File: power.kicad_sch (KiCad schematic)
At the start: 140 parts, among them Q10 SI7613DN-T1-GE3, Q2 BC817-25W, Q3 DZDH0401DW, Q4 DZDH0401DW, Q5 SI7613DN-T1-GE3, Q6 SI7613DN-T1-GE3, Q7 BC817-25W, Q8 BC817-25W, Q9 SI7613DN-T1-GE3, U1 LT8350RV#PBF, U2 MP2386GG, U3 TPS65983BAZBHR, U9 LM1117MP-25NOPB

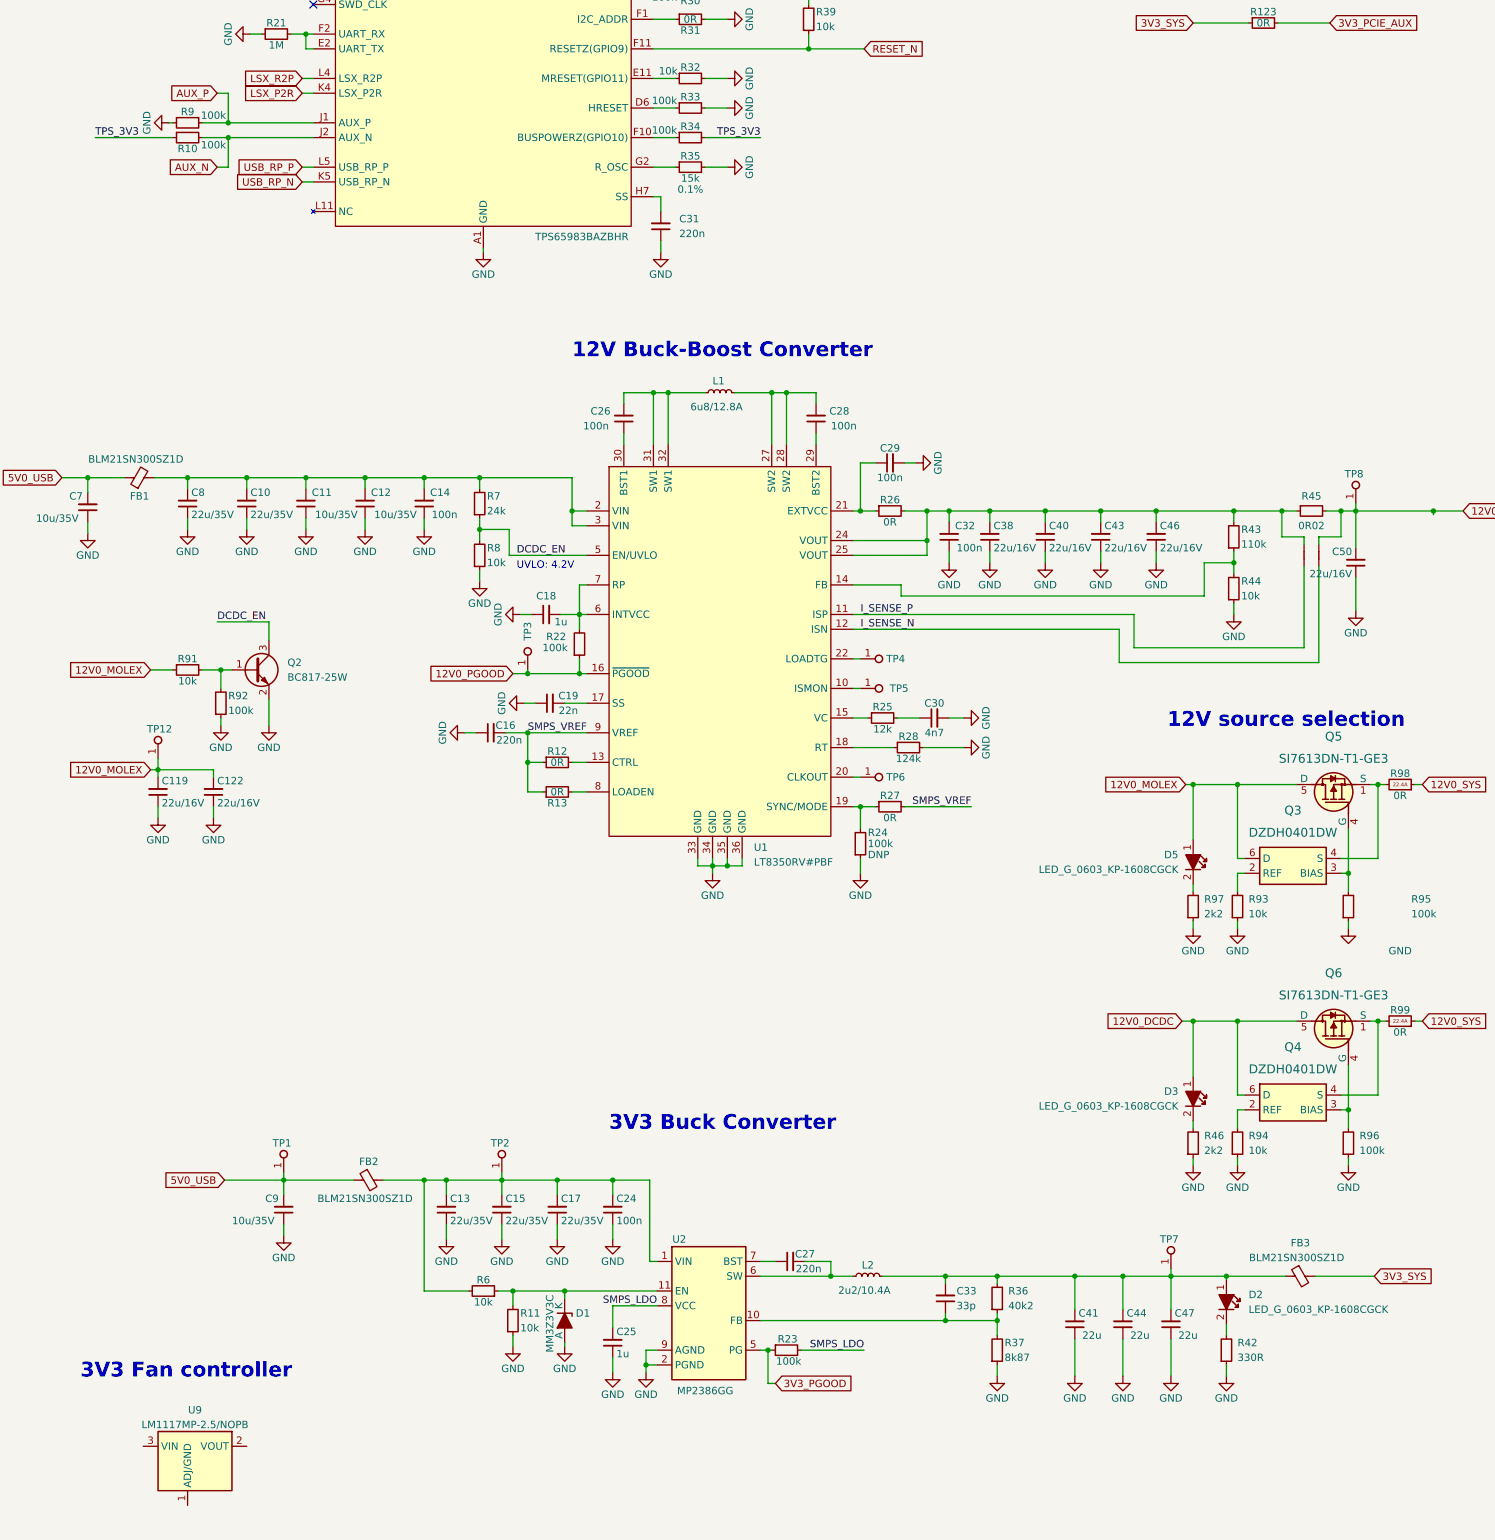
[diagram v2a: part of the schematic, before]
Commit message: Working on USB C HS routing
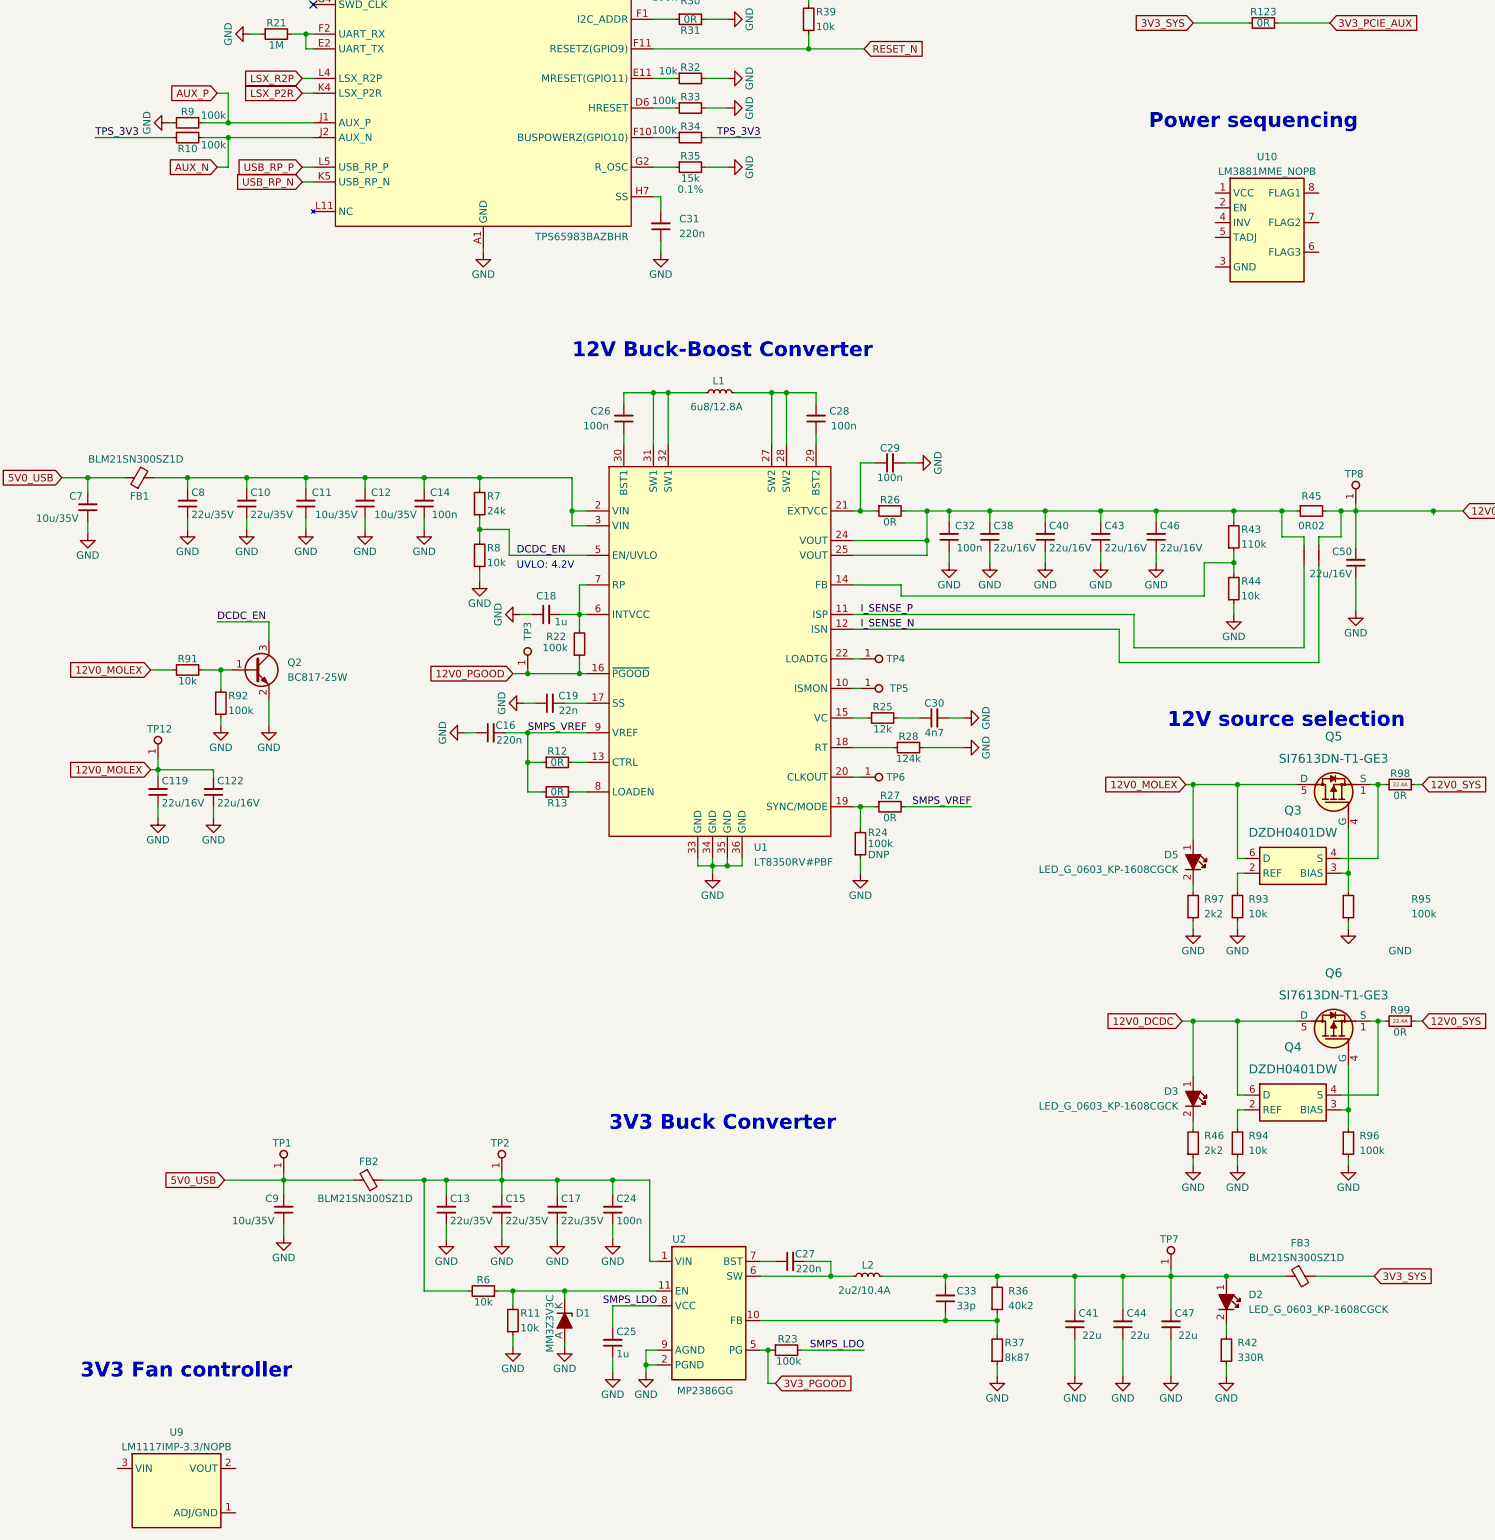
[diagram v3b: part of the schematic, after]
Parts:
- removed U9: LM1117MP-25NOPB, antmicro-footprints:SOT-223, symbol antmicroPMICVoltageRegulatorsLinear:LM1117MP-25NOPB
- added U10: LM3881MME_NOPB, antmicro-footprints:VSSOP-8_3x3mm_P0.65mm, symbol antmicroPMICPowerSequencers:LM3881MME_NOPB
- added U9: LM1117MP-3.3_NOPB, antmicro-footprints:SOT-223, symbol antmicroPMICVoltageRegulatorsLinear:LM1117MP-3.3_NOPB
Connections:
- new net: U9.2 (VOUT), U9.4 (VOUT)
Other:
- note added: "Power sequencing"
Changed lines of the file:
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@@
     (effects (font (size 2.54 2.54) bold) (justify left bottom))
   )
+  (text "Power sequencing" (at 216.535 149.86 0)
+    (effects (font (size 2.54 2.54) bold) (justify left bottom))
+  )
   (text "PCIE power" (at 228.6 22.225 0)
     (effects (font (size 2.54 2.54) bold) (justify left bottom))
@@
     (pin "2")
   )
-  (symbol (lib_id "antmicroPMICVoltageRegulatorsLinear:LM1117MP-25NOPB") (at 43.815 375.92 0) (unit 1)
-    (in_bom yes) (on_board yes) (fields_autoplaced)
-    (property "Reference" "U9" (id 0) (at 52.705 369.695 0)
-      (effects (font (size 1.27 1.27) (thickness 0.15)))
-    )
-    (property "Value" "LM1117MP-25NOPB" (id 1) (at 76.835 383.54 0)
-      (effects (font (size 1.27 1.27) (thickness 0.15)) (justify left bottom) hide)
-    )
-    (property "Footprint" "antmicro-footprints:SOT-223" (id 2) (at 76.835 386.08 0)
-      (effects (font (size 1.27 1.27) (thickness 0.15)) (justify left bottom) hide)
-    )
-    (property "Datasheet" "https://www.ti.com/general/docs/suppproductinfo.tsp?distId=26&gotoUrl=https://www.ti.com/lit/gpn/lm1117" (id 3) (at 76.835 388.62 0)
-      (effects (font (size 1.27 1.27) (thickness 0.15)) (justify left bottom) hide)
-    )
-    (property "MPN" "LM1117MP-2.5/NOPB" (id 4) (at 52.705 372.2187 0)
-      (effects (font (size 1.27 1.27) (thickness 0.15)))
-    )
-    (property "Manufacturer" "Texas Instruments" (id 5) (at 76.835 391.16 0)
-      (effects (font (size 1.27 1.27) (thickness 0.15)) (justify left bottom) hide)
-    )
-    (property "Author" "Antmicro" (id 6) (at 76.835 393.7 0)
-      (effects (font (size 1.27 1.27) (thickness 0.15)) (justify left bottom) hide)
-    )
-    (property "License" "Apache-2.0" (id 7) (at 76.835 396.24 0)
-      (effects (font (size 1.27 1.27) (thickness 0.15)) (justify left bottom) hide)
-    )
-    (pin "1")
-    (pin "2")
-    (pin "3")
-    (pin "4")
-  )
   (symbol (lib_name "C_22u_16V_0603_1") (lib_id "antmicroCapacitors0603:C_22u_16V_0603") (at 217.805 222.25 90) (unit 1)
     (in_bom yes) (on_board yes)
@@
     (pin "2")
   )
+  (symbol (lib_id "antmicroPMICPowerSequencers:LM3881MME_NOPB") (at 227.965 160.655 0) (unit 1)
+    (in_bom yes) (on_board yes) (fields_autoplaced)
+    (property "Reference" "U10" (id 0) (at 236.855 154.43 0)
+      (effects (font (size 1.27 1.27) (thickness 0.15)))
+    )
+    (property "Value" "LM3881MME_NOPB" (id 1) (at 236.855 156.9537 0)
+      (effects (font (size 1.27 1.27) (thickness 0.15)))
+    )
+    (property "Footprint" "antmicro-footprints:VSSOP-8_3x3mm_P0.65mm" (id 2) (at 271.145 168.275 0)
+      (effects (font (size 1.27 1.27) (thickness 0.15)) (justify left bottom) hide)
+    )
+    (property "Datasheet" "http://www.ti.com/lit/ds/symlink/lm3881.pdf" (id 3) (at 271.145 170.815 0)
+      (effects (font (size 1.27 1.27) (thickness 0.15)) (justify left bottom) hide)
+    )
+    (property "Manufacturer" "Texas Instruments" (id 4) (at 271.145 173.355 0)
+      (effects (font (size 1.27 1.27) (thickness 0.15)) (justify left bottom) hide)
+    )
+    (property "MPN" "LM3881MME/NOPB" (id 5) (at 271.145 175.895 0)
+      (effects (font (size 1.27 1.27) (thickness 0.15)) (justify left bottom) hide)
+    )
+    (property "Author" "Antmicro" (id 6) (at 271.145 178.435 0)
+      (effects (font (size 1.27 1.27) (thickness 0.15)) (justify left bottom) hide)
+    )
+    (property "License" "Apache-2.0" (id 7) (at 271.145 180.975 0)
+      (effects (font (size 1.27 1.27) (thickness 0.15)) (justify left bottom) hide)
+    )
+    (pin "1")
+    (pin "2")
+    (pin "3")
+    (pin "4")
+    (pin "5")
+    (pin "6")
+    (pin "7")
+    (pin "8")
+  )
   (symbol (lib_name "R_100k_0402_9") (lib_id "antmicroResistors0402:R_100k_0402") (at 234.95 62.23 90) (unit 1)
     (in_bom yes) (on_board yes)
@@
     (pin "1")
   )
+  (symbol (lib_id "antmicroPMICVoltageRegulatorsLinear:LM1117MP-3.3_NOPB") (at 39.37 379.73 0) (unit 1)
+    (in_bom yes) (on_board yes) (fields_autoplaced)
+    (property "Reference" "U9" (id 0) (at 49.53 373.505 0)
+      (effects (font (size 1.27 1.27) (thickness 0.15)))
+    )
+    (property "Value" "LM1117MP-3.3_NOPB" (id 1) (at 72.39 394.97 0)
+      (effects (font (size 1.27 1.27) (thickness 0.15)) (justify left bottom) hide)
+    )
+    (property "Footprint" "antmicro-footprints:SOT-223" (id 2) (at 72.39 397.51 0)
+      (effects (font (size 1.27 1.27) (thickness 0.15)) (justify left bottom) hide)
+    )
+    (property "Datasheet" "https://www.ti.com/lit/ds/symlink/lm1117.pdf?ts=1695352253515&ref_url=https%253A%252F%252Fwww.google.com%252F" (id 3) (at 72.39 400.05 0)
+      (effects (font (size 1.27 1.27) (thickness 0.15)) (justify left bottom) hide)
+    )
+    (property "Author" "Antmicro" (id 4) (at 72.39 384.81 0)
+      (effects (font (size 1.27 1.27) (thickness 0.15)) (justify left bottom) hide)
+    )
+    (property "License" "Apache-2.0" (id 5) (at 72.39 387.35 0)
+      (effects (font (size 1.27 1.27) (thickness 0.15)) (justify left bottom) hide)
+    )
+    (property "MPN" "LM1117IMP-3.3/NOPB" (id 6) (at 49.53 376.0287 0)
+      (effects (font (size 1.27 1.27) (thickness 0.15)))
+    )
+    (property "Manufacturer" "Texas Instruments" (id 7) (at 72.39 392.43 0)
+      (effects (font (size 1.27 1.27) (thickness 0.15)) (justify left bottom) hide)
+    )
+    (pin "1")
+    (pin "2")
+    (pin "3")
+    (pin "4")
+  )
   (symbol (lib_id "antmicropower:GND") (at 252.095 232.41 0) (unit 1)

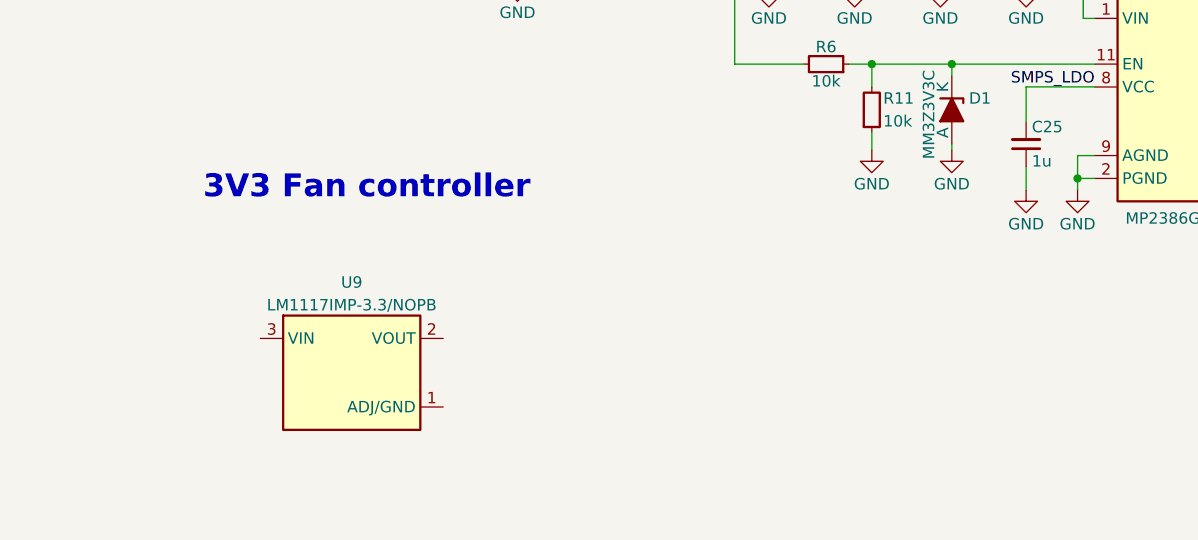
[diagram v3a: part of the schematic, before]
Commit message: Redesigned power circuitry for the fan controller
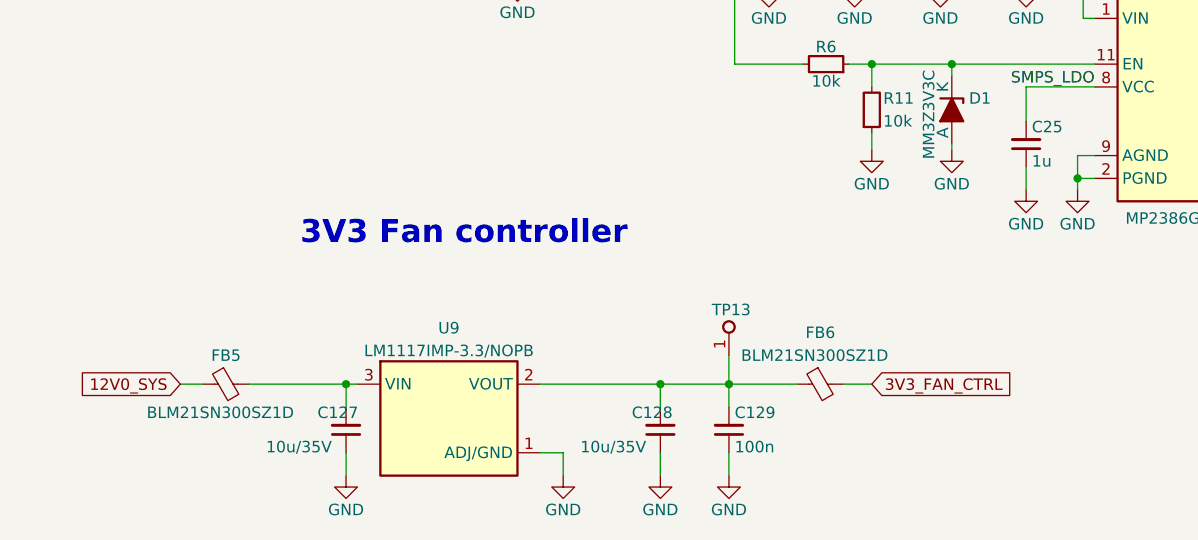
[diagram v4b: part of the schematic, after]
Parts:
- added C127, C128: C_10u_0805_35V, antmicro-footprints:C_0805_2012Metric, symbol antmicroCapacitorsmisc:C_10u_0805_35V
- added C129: C_100n_0402, antmicro-footprints:C_0402_1005Metric, symbol antmicroCapacitors0402:C_100n_0402
- added FB5, FB6: BLM21SN300SZ1D, antmicro-footprints:FB_0805_2012Metric, symbol antmicroFerriteBeadsandChips:BLM21SN300SZ1D
- added TP13: TP_1mm_SMD, antmicro-footprints:Testpoint_smd_1mm, symbol antmicroTestPoints:TP_1mm_SMD
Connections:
- net 12V0_SYS: now also FB5.1
- net GND: now also U9.1 (ADJ/GND), C127.1, C128.1, C129.1
- net at U9.2 (VOUT), U9.4 (VOUT): now also C128.2, C129.2, FB6.1, TP13.1
- net at U9.3 (VIN): now also C127.2, FB5.2
- new net 3V3_FAN_CTRL: FB6.2
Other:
- moved on the sheet: U9
